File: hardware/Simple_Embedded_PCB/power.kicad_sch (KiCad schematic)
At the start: 32 parts, among them J7 5.5mm X 2.1mm Jack, Q2 AO3401A, U2 LMR16020PDDA, U3 AMS1117-3.3

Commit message: Added JLCPCB part numbers
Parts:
- C10, C11, C18, C20, C21, C22: LCSC Part Number (none) -> C13585
- C12: LCSC Part Number (none) -> C14663
- C13: LCSC Part Number (none) -> C440198
- C14, C15, C17, C19: LCSC Part Number (none) -> C307331
- C16: LCSC Part Number (none) -> C13533
- D3, D4, D5: LCSC Part Number (none) -> C2297
- D6: LCSC Part Number (none) -> C235988
- D7: LCSC Part Number (none) -> C8678
- L1: LCSC Part Number (none) -> C78804
- Q2: LCSC Part Number (none) -> C15127
- R10: LCSC Part Number (none) -> C23025
- R11: LCSC Part Number (none) -> C23228
- R12: LCSC Part Number (none) -> C25803
- R13: LCSC Part Number (none) -> C4190
- R14: LCSC Part Number (none) -> C25756
- R15: LCSC Part Number (none) -> C25741
- R16: LCSC Part Number (none) -> C226819
- R17, R18: LCSC Part Number (none) -> C25197
- U2: LCSC Part Number (none) -> C190006
- U3: LCSC Part Number (none) -> C6186
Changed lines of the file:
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@@
+      (effects (font (size 1.27 1.27)) hide)
+    )
+    (property "LCSC Part Number" "C13585" (id 4) (at 242.57 104.14 0)
       (effects (font (size 1.27 1.27)) hide)
     )
@@
       (effects (font (size 1.27 1.27)) hide)
     )
+    (property "LCSC Part Number" "C2297" (id 4) (at 86.36 118.11 0)
+      (effects (font (size 1.27 1.27)) hide)
+    )
     (pin "1")
     (pin "2")
@@
     )
     (property "Datasheet" "~" (id 3) (at 72.39 118.11 0)
+      (effects (font (size 1.27 1.27)) hide)
+    )
+    (property "LCSC Part Number" "C2297" (id 4) (at 72.39 118.11 0)
       (effects (font (size 1.27 1.27)) hide)
     )
@@
       (effects (font (size 1.27 1.27)) hide)
     )
+    (property "LCSC Part Number" "C4190" (id 4) (at 86.36 109.22 0)
+      (effects (font (size 1.27 1.27)) hide)
+    )
     (pin "1")
     (pin "2")
@@
     )
     (property "Datasheet" "~" (id 3) (at 242.57 110.49 0)
+      (effects (font (size 1.27 1.27)) hide)
+    )
+    (property "LCSC Part Number" "C25197" (id 4) (at 242.57 110.49 0)
       (effects (font (size 1.27 1.27)) hide)
     )
@@
       (effects (font (size 1.27 1.27)) hide)
     )
+    (property "LCSC Part Number" "C226819" (id 4) (at 227.33 62.23 0)
+      (effects (font (size 1.27 1.27)) hide)
+    )
     (pin "1")
     (pin "2")
@@
       (effects (font (size 1.27 1.27)) hide)
     )
+    (property "LCSC Part Number" "C2297" (id 4) (at 58.42 118.11 0)
+      (effects (font (size 1.27 1.27)) hide)
+    )
     (pin "1")
     (pin "2")
@@
       (effects (font (size 1.27 1.27)) hide)
     )
+    (property "LCSC Part Number" "C13585" (id 4) (at 250.19 54.61 0)
+      (effects (font (size 1.27 1.27)) hide)
+    )
     (pin "1")
     (pin "2")
@@
     )
     (property "Datasheet" "~" (id 3) (at 261.62 54.61 0)
+      (effects (font (size 1.27 1.27)) hide)
+    )
+    (property "LCSC Part Number" "C13585" (id 4) (at 261.62 54.61 0)
       (effects (font (size 1.27 1.27)) hide)
     )
@@
     (property "temperature range low" "-40°C" (id 31) (at 152.4 -36.83 0)
       (effects (font (size 1.27 1.27)) (justify left) hide)
+    )
+    (property "LCSC Part Number" "C190006" (id 32) (at 152.4 46.99 0)
+      (effects (font (size 1.27 1.27)) hide)
     )
     (pin "1")
@@
       (effects (font (size 1.27 1.27)) hide)
     )
+    (property "LCSC Part Number" "C25741" (id 4) (at 227.33 54.61 0)
+      (effects (font (size 1.27 1.27)) hide)
+    )
     (pin "1")
     (pin "2")
@@
     )
     (property "Datasheet" "~" (id 3) (at 72.39 109.22 0)
+      (effects (font (size 1.27 1.27)) hide)
+    )
+    (property "LCSC Part Number" "C23228" (id 4) (at 72.39 109.22 0)
       (effects (font (size 1.27 1.27)) hide)
     )
@@
       (effects (font (size 1.27 1.27)) hide)
     )
+    (property "LCSC Part Number" "C78804" (id 4) (at 212.09 50.8 0)
+      (effects (font (size 1.27 1.27)) hide)
+    )
     (pin "1")
     (pin "2")
@@
       (effects (font (size 1.27 1.27)) hide)
     )
+    (property "LCSC Part Number" "C25756" (id 4) (at 132.08 60.96 0)
+      (effects (font (size 1.27 1.27)) hide)
+    )
     (pin "1")
     (pin "2")
@@
     )
     (property "Datasheet" "~" (id 3) (at 231.14 110.49 0)
+      (effects (font (size 1.27 1.27)) hide)
+    )
+    (property "LCSC Part Number" "C25197" (id 4) (at 231.14 110.49 0)
       (effects (font (size 1.27 1.27)) hide)
     )
@@
       (effects (font (size 1.27 1.27)) hide)
     )
+    (property "LCSC Part Number" "C6186" (id 4) (at 208.28 100.33 0)
+      (effects (font (size 1.27 1.27)) hide)
+    )
     (pin "1")
     (pin "2")
@@
       (effects (font (size 1.27 1.27)) hide)
     )
+    (property "LCSC Part Number" "C307331" (id 5) (at 199.39 46.99 0)
+      (effects (font (size 1.27 1.27)) hide)
+    )
     (pin "1")
     (pin "2")
@@
       (effects (font (size 1.27 1.27)) hide)
     )
+    (property "LCSC Part Number" "C13585" (id 4) (at 101.6 53.34 0)
+      (effects (font (size 1.27 1.27)) hide)
+    )
     (pin "1")
     (pin "2")
@@
       (effects (font (size 1.27 1.27)) hide)
     )
+    (property "LCSC Part Number" "C23025" (id 4) (at 58.42 109.22 0)
+      (effects (font (size 1.27 1.27)) hide)
+    )
     (pin "1")
     (pin "2")
@@
       (effects (font (size 1.27 1.27)) hide)
     )
+    (property "LCSC Part Number" "C307331" (id 4) (at 193.04 104.14 0)
+      (effects (font (size 1.27 1.27)) hide)
+    )
     (pin "1")
     (pin "2")
@@
     )
     (property "Datasheet" "~" (id 3) (at 231.14 104.14 0)
+      (effects (font (size 1.27 1.27)) hide)
+    )
+    (property "LCSC Part Number" "C13585" (id 4) (at 231.14 104.14 0)
       (effects (font (size 1.27 1.27)) hide)
     )
@@
       (effects (font (size 1.27 1.27)) hide)
     )
+    (property "LCSC Part Number" "C15127" (id 4) (at 80.01 49.53 0)
+      (effects (font (size 1.27 1.27)) hide)
+    )
     (pin "1")
     (pin "2")
@@
     )
     (property "Datasheet" "~" (id 3) (at 181.61 104.14 0)
+      (effects (font (size 1.27 1.27)) hide)
+    )
+    (property "LCSC Part Number" "C440198" (id 4) (at 181.61 104.14 0)
       (effects (font (size 1.27 1.27)) hide)
     )
@@
       (effects (font (size 1.27 1.27)) hide)
     )
+    (property "LCSC Part Number" "C235988" (id 4) (at 87.63 52.07 0)
+      (effects (font (size 1.27 1.27)) hide)
+    )
     (pin "1")
     (pin "2")
@@
       (effects (font (size 1.27 1.27)) hide)
     )
+    (property "LCSC Part Number" "C8678" (id 4) (at 201.93 55.88 0)
+      (effects (font (size 1.27 1.27)) hide)
+    )
     (pin "1")
     (pin "2")
@@
       (effects (font (size 1.27 1.27)) hide)
     )
+    (property "LCSC Part Number" "C13533" (id 4) (at 215.9 54.61 0)
+      (effects (font (size 1.27 1.27)) hide)
+    )
     (pin "1")
     (pin "2")
@@
     )
     (property "Datasheet" "~" (id 3) (at 218.44 104.14 0)
+      (effects (font (size 1.27 1.27)) hide)
+    )
+    (property "LCSC Part Number" "C307331" (id 4) (at 218.44 104.14 0)
       (effects (font (size 1.27 1.27)) hide)
     )
@@
       (effects (font (size 1.27 1.27)) hide)
     )
+    (property "LCSC Part Number" "C14663" (id 4) (at 121.92 53.34 0)
+      (effects (font (size 1.27 1.27)) hide)
+    )
     (pin "1")
     (pin "2")
@@
       (effects (font (size 1.27 1.27)) hide)
     )
+    (property "LCSC Part Number" "C13585" (id 4) (at 111.76 53.34 0)
+      (effects (font (size 1.27 1.27)) hide)
+    )
     (pin "1")
     (pin "2")
@@
       (effects (font (size 1.27 1.27)) hide)
     )
+    (property "LCSC Part Number" "C307331" (id 4) (at 238.76 54.61 0)
+      (effects (font (size 1.27 1.27)) hide)
+    )
     (pin "1")
     (pin "2")
@@
       (effects (font (size 1.27 1.27)) hide)
     )
+    (property "LCSC Part Number" "C25803" (id 4) (at 80.01 59.69 0)
+      (effects (font (size 1.27 1.27)) hide)
+    )

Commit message: Board ordered!  Created Gerber files, drill files, BOM, and parts placement file.
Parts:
- R17, R18: LCSC Part Number C25197 -> C22936
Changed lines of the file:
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@@
       (effects (font (size 1.27 1.27)) hide)
     )
-    (property "LCSC Part Number" "C25197" (id 4) (at 242.57 110.49 0)
+    (property "LCSC Part Number" "C22936" (id 4) (at 242.57 110.49 0)
       (effects (font (size 1.27 1.27)) hide)
     )
@@
       (effects (font (size 1.27 1.27)) hide)
     )
-    (property "LCSC Part Number" "C25197" (id 4) (at 231.14 110.49 0)
-      (effects (font (size 1.27 1.27)) hide)
-    )
+    (property "LCSC Part Number" "C22936" (id 4) (at 231.14 110.49 0)
+      (effects (font (size 1.27 1.27)) hide)
+    )

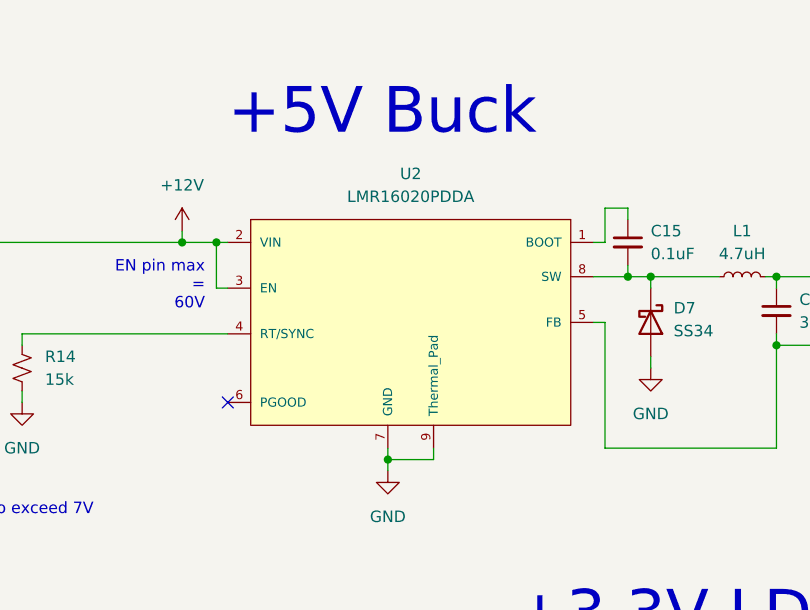
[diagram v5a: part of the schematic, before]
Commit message: Changed KiCad project to use symbols, footprints, and 3D models from project itself.
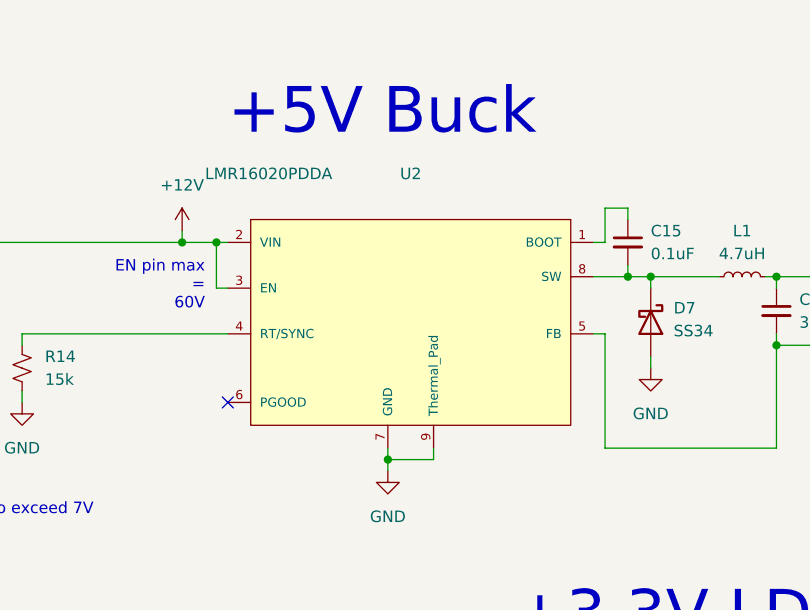
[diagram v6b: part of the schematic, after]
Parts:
- L1: footprint MySO:SUNLORD_SWPA6045S4R7MT -> Simple_Embedded_PCB:SUNLORD_SWPA6045S4R7MT
- U2: footprint MySO:8-PowerSOIC -> Simple_Embedded_PCB:8-PowerSOIC; symbol LMR16020PDDAR:LMR16020PDDA -> Simple_Embedded_PCB:LMR16020PDDA; LCSC Part Number C190006 -> (none); switching frequency 1.5 MHz -> 200-2500kHz
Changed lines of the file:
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@@
-    (stroke (width 0) (type default) (color 0 0 0 0))
-  )
-  (wire (pts (xy 196.85 55.88) (xy 196.85 69.85))
     (stroke (width 0) (type default) (color 0 0 0 0))
   )
@@
     (stroke (width 0) (type default) (color 0 0 0 0))
   )
-  (wire (pts (xy 195.58 55.88) (xy 196.85 55.88))
-    (stroke (width 0) (type default) (color 0 0 0 0))
-  )
   (wire (pts (xy 153.67 46.99) (xy 154.94 46.99))
     (stroke (width 0) (type default) (color 0 0 0 0))
@@
     (stroke (width 0) (type default) (color 0 0 0 0))
   )
+  (wire (pts (xy 196.85 69.85) (xy 196.85 57.15))
+    (stroke (width 0) (type default) (color 0 0 0 0))
+  )
   (wire (pts (xy 199.39 44.45) (xy 199.39 43.18))
     (stroke (width 0) (type default) (color 0 0 0 0))
@@
   )
   (wire (pts (xy 177.8 69.85) (xy 177.8 71.12))
+    (stroke (width 0) (type default) (color 0 0 0 0))
+  )
+  (wire (pts (xy 196.85 57.15) (xy 195.58 57.15))
     (stroke (width 0) (type default) (color 0 0 0 0))
   )
@@
     (pin "1")
   )
-  (symbol (lib_id "LMR16020PDDAR:LMR16020PDDA") (at 152.4 46.99 0) (unit 1)
+  (symbol (lib_id "Simple_Embedded_PCB:LMR16020PDDA") (at 152.4 46.99 0) (unit 1)
     (in_bom yes) (on_board yes) (fields_autoplaced)
     (property "Reference" "U2" (id 0) (at 175.26 39.37 0))
-    (property "Value" "LMR16020PDDA" (id 1) (at 175.26 41.91 0))
-    (property "Footprint" "MySO:8-PowerSOIC" (id 2) (at 152.4 36.83 0)
+    (property "Value" "LMR16020PDDA" (id 1) (at 152.4 39.37 0)
+      (effects (font (size 1.27 1.27)) (justify left))
+    )
+    (property "Footprint" "Simple_Embedded_PCB:8-PowerSOIC" (id 2) (at 152.4 36.83 0)
       (effects (font (size 1.27 1.27)) (justify left) hide)
     )
@@
       (effects (font (size 1.27 1.27)) (justify left) hide)
     )
-    (property "switching frequency" "1.5 MHz" (id 28) (at 152.4 -29.21 0)
+    (property "switching frequency" "200-2500kHz" (id 28) (at 152.4 -29.21 0)
       (effects (font (size 1.27 1.27)) (justify left) hide)
     )
@@
     (property "temperature range low" "-40°C" (id 31) (at 152.4 -36.83 0)
       (effects (font (size 1.27 1.27)) (justify left) hide)
-    )
-    (property "LCSC Part Number" "C190006" (id 32) (at 152.4 46.99 0)
-      (effects (font (size 1.27 1.27)) hide)
     )
     (pin "1")
@@
     (property "Reference" "L1" (id 0) (at 212.09 45.72 90))
     (property "Value" "4.7uH" (id 1) (at 212.09 48.26 90))
-    (property "Footprint" "MySO:SUNLORD_SWPA6045S4R7MT" (id 2) (at 212.09 50.8 0)
-      (effects (font (size 1.27 1.27)) hide)
-    )
+    (property "Footprint" "Simple_Embedded_PCB:SUNLORD_SWPA6045S4R7MT" (id 2) (at 212.09 50.8 0)
+      (effects (font (size 1.27 1.27)) hide)
+    )
